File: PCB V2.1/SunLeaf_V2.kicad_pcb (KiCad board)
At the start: 2 copper layers, 118 parts, among them IC1 ESP_09, J1 20021121-00010C4LF, J10 S4B-PH-SM4-TB(LF)(SN), J11 S4B-PH-SM4-TB(LF)(SN), J12 S4B-PH-SM4-TB(LF)(SN), J13 S4B-PH-SM4-TB(LF)(SN), J14 S4B-PH-SM4-TB(LF)(SN), J15 S4B-PH-SM4-TB(LF)(SN), J16 S4B-PH-SM4-TB(LF)(SN), J2 0475890001-MicroUSBPort, J3 S2B-PH-SM4-TB(LF)(SN), J4 S3B-PH-SM4-TB(LF)(SN), J5 S4B-PH-SM4-TB(LF)(SN), J6 S4B-PH-SM4-TB(LF)(SN), J7 S4B-PH-SM4-TB(LF)(SN), J8 S4B-PH-SM4-TB(LF)(SN), J9 S4B-PH-SM4-TB(LF)(SN), P1 CONN_01X04, Q1 DMG2307L-7, Q2 DMG2307L-7, SW1 B3U-1000P, SW2 B3U-1000P, T1 1909763-1, U1 STM32F446RET6_-_TQFP64, U2 BQ24210DQCT, U3 AZ1117CR-3.3TRG1_1, U4 74HC4052D, U5 PCA9518DBQR, X1 ABM3B8.000MHZB2T, X2 ABS07-32.768KHZ-9-T

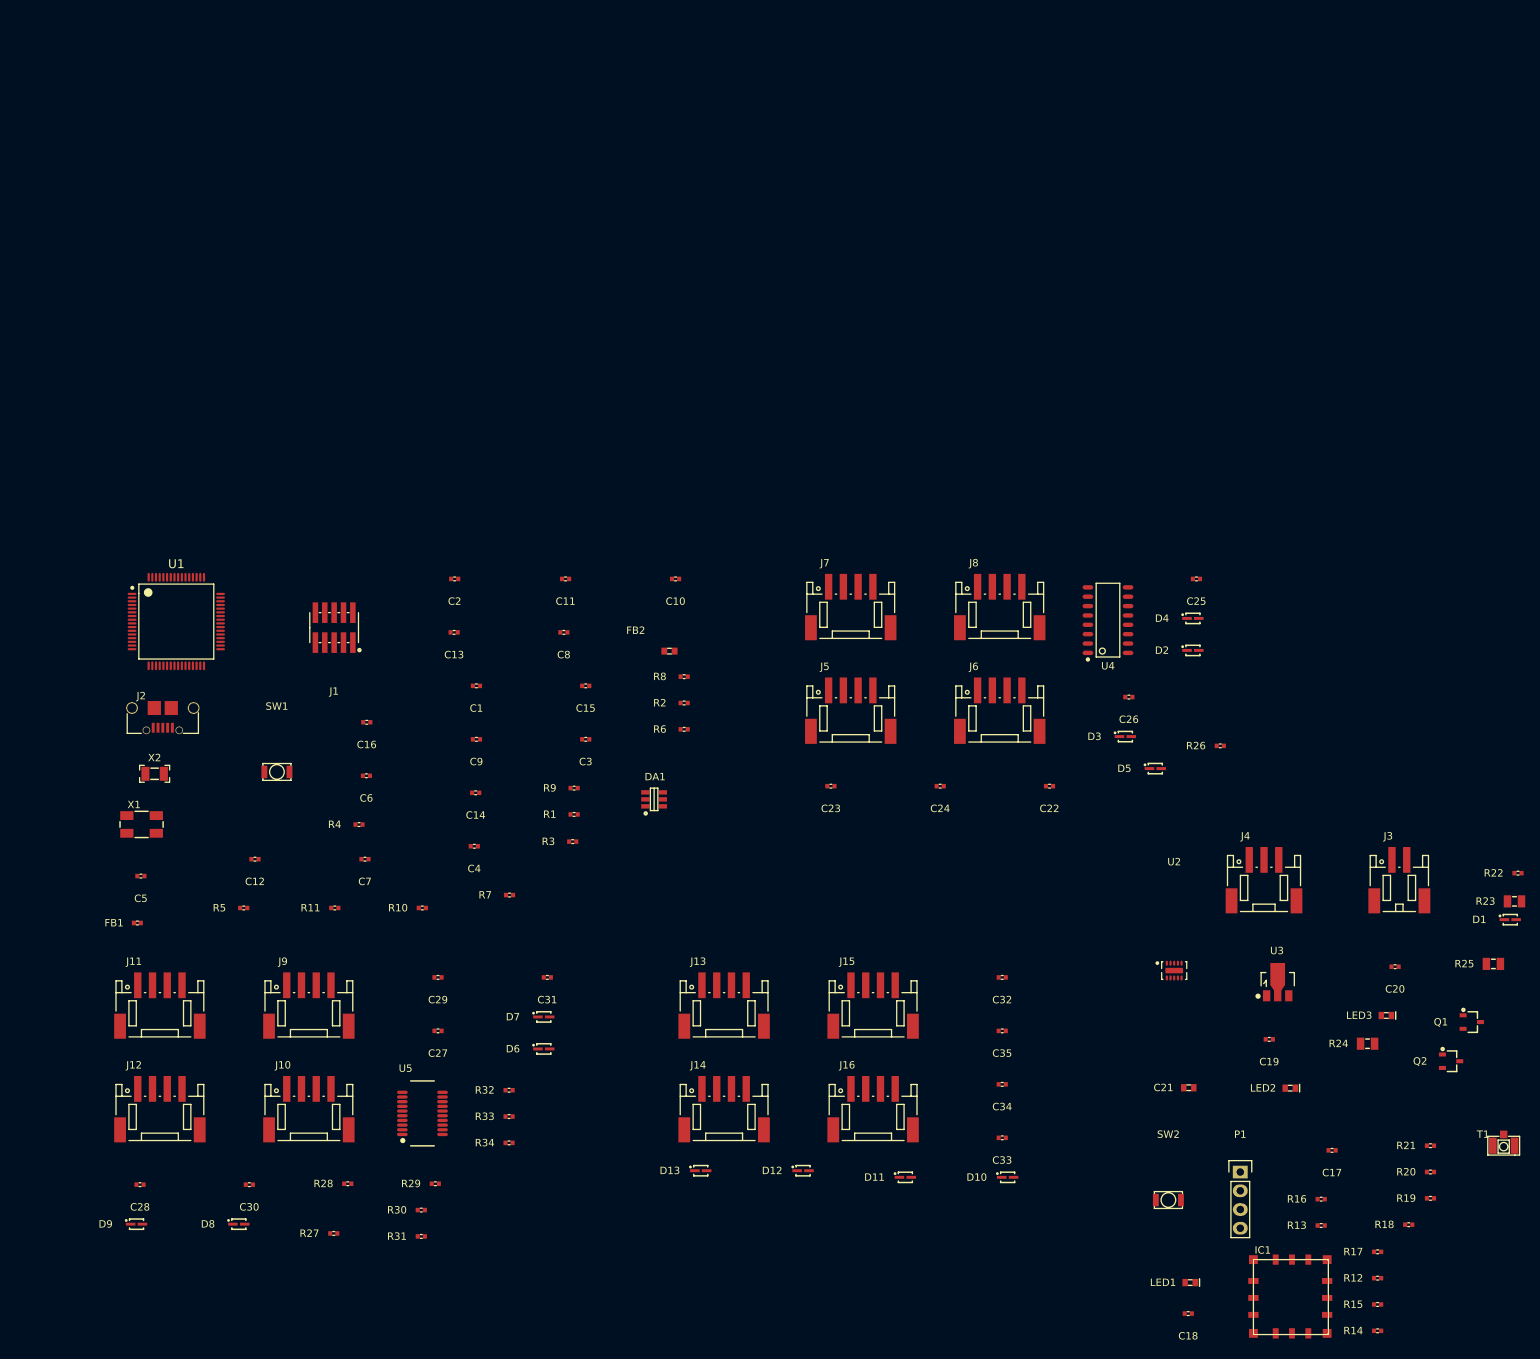
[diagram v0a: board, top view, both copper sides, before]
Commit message: Placement
Heavy progress on component placement in KiCAD for SunLEaf V2,
committing to save progress, nightly builds of KiCAD are very crash
prone.
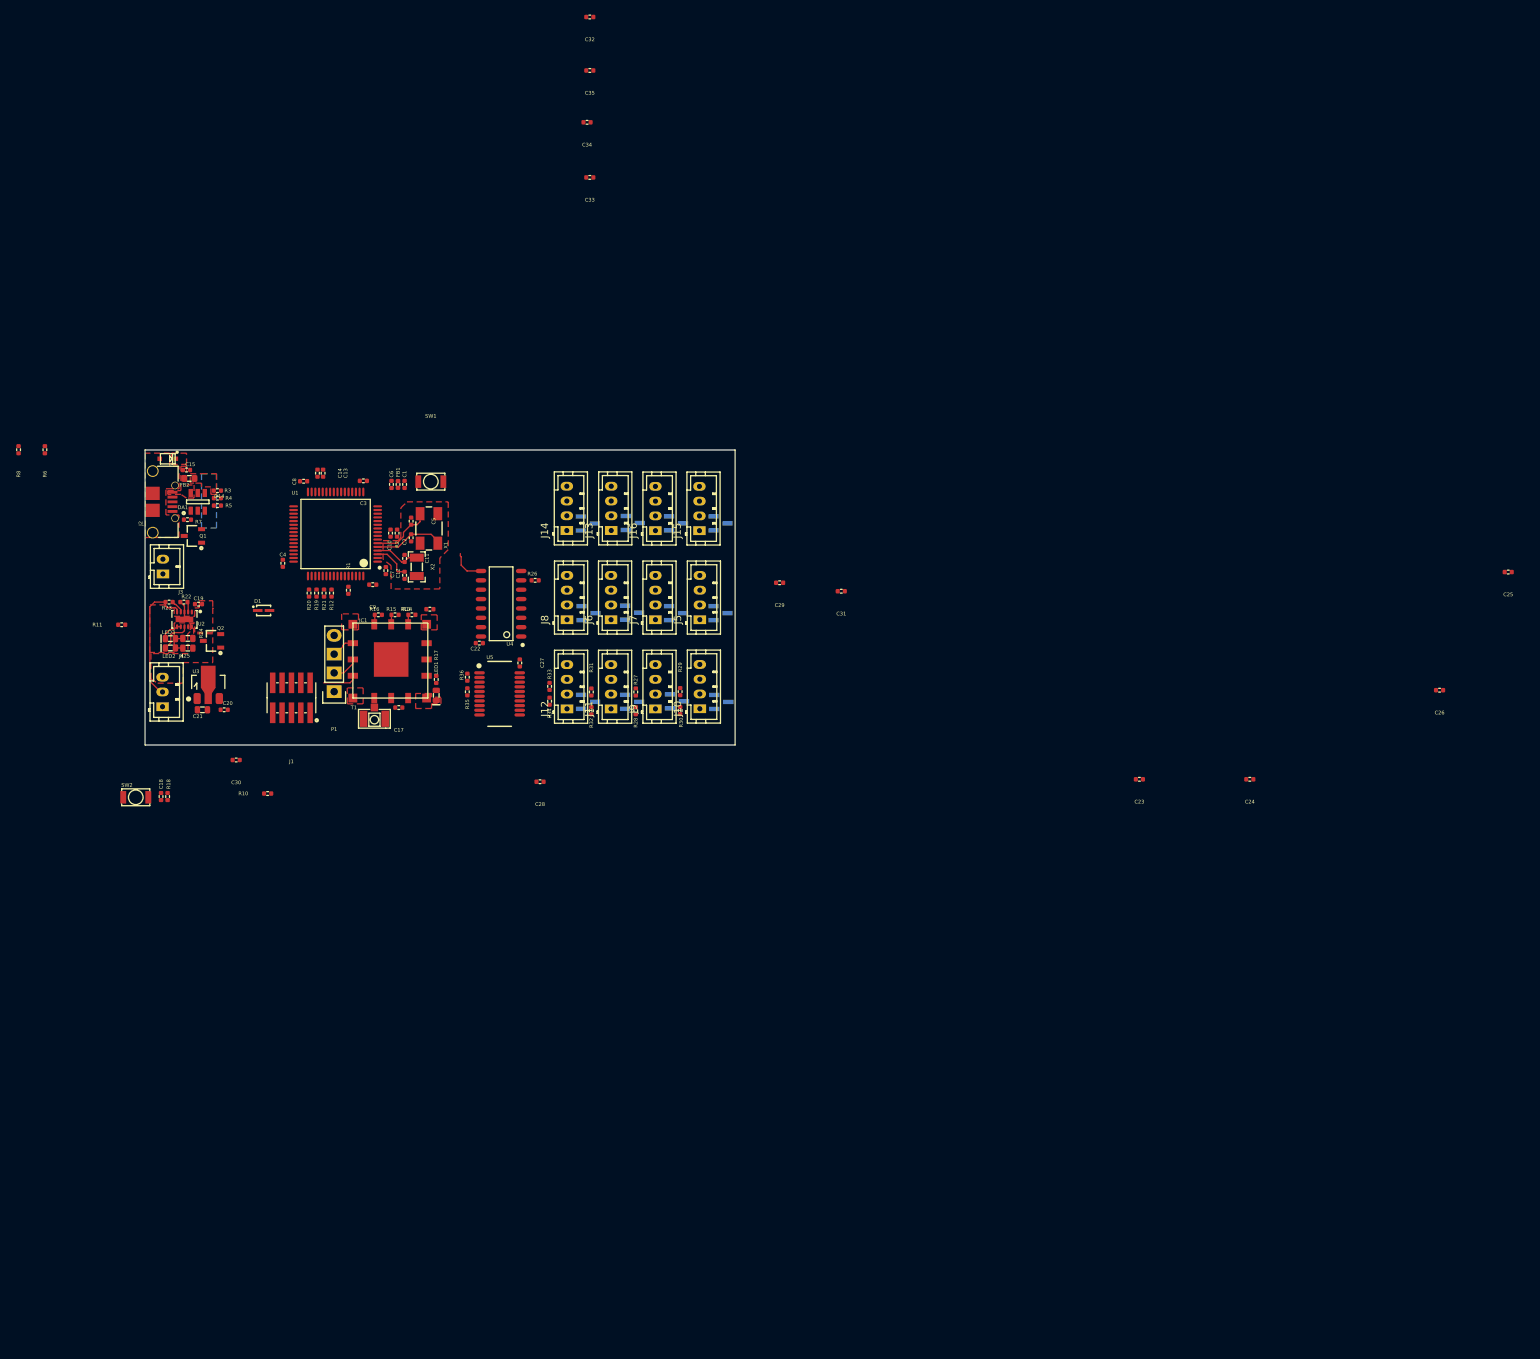
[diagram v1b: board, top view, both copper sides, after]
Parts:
- removed C16: CL05C470FB5NNNC, PCB_Footprints:C0402
- removed R9: RC1005F105CS, PCB_Footprints:R0402
- added D14: RSB39VTE-17, PCB_Footprints:RSB39VTE-17, F.Cu at (43.1, 31.2)
- added R35: RC1005F472CS, PCB_Footprints:R0402, F.Cu at (83.7, 62.8)
- added R36: RC1005F472CS, PCB_Footprints:R0402, F.Cu at (83.7, 60.8)
- D10, D11, D12, D13, D2, D3, D4, D5, D6, D7, D8, D9: footprint PCB_Footprints:BAT20JFILM -> PCB_Footprints:PESD3V3L2BT,215; moved to B.Cu
- J10, J11, J12, J13, J14, J15, J16, J5, J6, J7, J8, J9: value S4B-PH-SM4-TB(LF)(SN) -> B4B-PH-K-S(LF)(SN); footprint PCB_Footprints:S4B-PH-SM4-TB(LF)(SN) -> PCB_Footprints:B4B-PH-K-S(LF)(SN)
- J3: value S2B-PH-SM4-TB(LF)(SN) -> B2B-PH-K-S(LF)(SN); footprint PCB_Footprints:S2B-PH-SM4-TB(LF)(SN) -> PCB_Footprints:B2B-PH-K-S(LF)(SN)
- J4: value S3B-PH-SM4-TB(LF)(SN) -> B3B-PH-K-S(LF)(SN); footprint PCB_Footprints:S3B-PH-SM4-TB(LF)(SN) -> PCB_Footprints:B3B-PH-K-S(LF)(SN)
- R23: value RC2012F202CS -> RC1005F102CS; footprint PCB_Footprints:R0805 -> PCB_Footprints:R0402
- R24, R25: value RC2012F202CS -> RC1608J202CS; footprint PCB_Footprints:R0805 -> PCB_Footprints:R0603
- moved R23 186.9 mm to (43.3, 50.6), turned to 180 degrees
- moved Q1 185.5 mm to (46.5, 41.7), turned to 180 degrees
- moved R22 184.6 mm to (45.3, 50.6), turned to 180 degrees
- moved R25 182.4 mm to (45.8, 55.5)
- moved R18 178.0 mm to (43.1, 77.0), turned to 90 degrees
- moved Q2 177.4 mm to (49.1, 55.9), turned to 180 degrees
- moved D1 174.1 mm to (56.1, 51.8)
- moved J3 172.7 mm to (42.4, 46.8), turned to 90 degrees
- moved LED3 172.6 mm to (43.4, 55.6), turned to 180 degrees
- moved R19 171.9 mm to (63.2, 49.4), turned to 90 degrees
- moved R20 171.1 mm to (62.2, 49.4), turned to 90 degrees
- moved R12 169.5 mm to (65.3, 49.4), turned to 270 degrees
- moved R24 168.7 mm to (45.8, 56.9)
- moved R21 167.7 mm to (64.3, 49.4), turned to 90 degrees
- moved T1 163.7 mm to (71.1, 66.4)
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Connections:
- net Net-(D2-Pad1) renamed /UART Grove Sensors/UART_RX3
- net Net-(D2-Pad2) renamed /UART Grove Sensors/UART_TX3
- net Net-(D3-Pad1) renamed /UART Grove Sensors/UART_RX2
- net Net-(D3-Pad2) renamed /UART Grove Sensors/UART_TX2
- net Net-(D4-Pad1) renamed /UART Grove Sensors/UART_RX1
- net Net-(D4-Pad2) renamed /UART Grove Sensors/UART_TX1
- net Net-(D5-Pad1) renamed /UART Grove Sensors/UART_RX0
- net Net-(D5-Pad2) renamed /UART Grove Sensors/UART_TX0
- C17 pad 1: Net-(C17-Pad1) -> +3V3
- C19 pad 1: Net-(C19-Pad1) -> /MCU-STM32F446RET6/VBUS
- C8 pad 1: Net-(C8-Pad1) -> +3V3
- IC1 pad 15: Net-(C17-Pad1) -> +3V3
- J2 pad 5: Net-(J2-Pad5) -> GND
- J2 pad 6: Net-(C16-Pad1) -> Net-(D14-Pad1)
- J2 pad 8: Net-(C16-Pad1) -> Net-(D14-Pad1)
- J2 pad 9: Net-(C16-Pad1) -> Net-(D14-Pad1)
- J3 pad 1: Net-(J3-Pad1) -> GND
- J3 pad 2: GND -> Net-(J3-Pad2)
- J4 pad 1: /Power-System/BAT -> GND
- J4 pad 3: GND -> /Power-System/BAT
- P1 pad 1: Net-(IC1-Pad11) -> GND
- P1 pad 2: Net-(IC1-Pad10) -> Net-(IC1-Pad11)
- P1 pad 3: /WiFi-ESP8266-ESP-09/PGM_MODE -> Net-(IC1-Pad10)
- P1 pad 4: GND -> /WiFi-ESP8266-ESP-09/PGM_MODE
- Q1 pad 2: Net-(Q1-Pad2) -> /MCU-STM32F446RET6/VBUS
- Q1 pad 3: Net-(J3-Pad1) -> Net-(J3-Pad2)
- R23 pad 1: /Power-System/THERM -> Net-(R23-Pad1)
- R23 pad 2: Net-(R23-Pad2) -> /Power-System/THERM
- R24 pad 1: /Power-System/BAT -> Net-(LED2-Pad1)
- R24 pad 2: Net-(LED2-Pad1) -> /Power-System/BAT
- R25 pad 1: /Power-System/BAT -> Net-(LED3-Pad1)
- R25 pad 2: Net-(LED3-Pad1) -> /Power-System/BAT
- U1 pad 1: Net-(C8-Pad1) -> +3V3
- U2 pad 4: Net-(R23-Pad2) -> Net-(R23-Pad1)
- X1 pad 2: Net-(C5-Pad1) -> GND
- X1 pad 3: GND -> Net-(C5-Pad1)
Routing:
- net /Power-System/THERM: track 0.00 -> 17.5 mm
- net Net-(C2-Pad1): track 0.00 -> 9.54 mm
- net Net-(C5-Pad1): track 0.00 -> 8.37 mm
- net Net-(C11-Pad1): track 0.00 -> 6.22 mm
- net Net-(C12-Pad1): track 0.00 -> 5.18 mm
- net Net-(C18-Pad1): track 0.00 -> 4.69 mm
- net Net-(LED2-Pad2): track 0.00 -> 4.68 mm
- net /MCU-STM32F446RET6/USW_S1: track 0.00 -> 4.63 mm
- net Net-(IC1-Pad11): track 0.00 -> 3.63 mm
- net Net-(IC1-Pad10): track 0.00 -> 3.24 mm
- net Net-(LED3-Pad2): track 0.00 -> 3.10 mm
- net GND: track 0.00 -> 2.58 mm
- net Net-(R23-Pad1): track 0.00 -> 1.85 mm
- net Net-(R22-Pad1): track 0.00 -> 1.38 mm
- net /WiFi-ESP8266-ESP-09/PGM_MODE: track 0.00 -> 1.32 mm
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- added copper zone on B.Cu, net /MCU-STM32F446RET6/VBUS
- added copper zone on F.Cu, net /MCU-STM32F446RET6/VBUS
- added copper zone on F.Cu, net /Power-System/BAT
- added copper zone on F.Cu, net GND
- added copper zone on F.Cu, net Net-(C15-Pad2)
- added copper zone on F.Cu, net Net-(D14-Pad1)
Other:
- board outline added: 80 x 40 mm
- copper layers 2 -> 4
- net class All added: clearance 0.1524, trace_width 0.1778, via_dia 0.635, via_drill 0.3302
- net class Default: clearance 0.2 -> 0.1524; trace_width 0.25 -> 0.1778; via_dia 0.6 -> 0.635; via_drill 0.4 -> 0.3302
- rule pad_to_mask_clearance: 0.2 -> 0
- rule trace_clearance: 0.2 -> 0.1524
- rule trace_min: 0.2 -> 0.1778
- rule via_min_drill: 0.3 -> 0.3302
- rule via_min_size: 0.4 -> 0.635

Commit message: Placement progress
Placement is 99% done board is being resized. Next commit TVS diode
pairs will be fliped and the baord further resized.
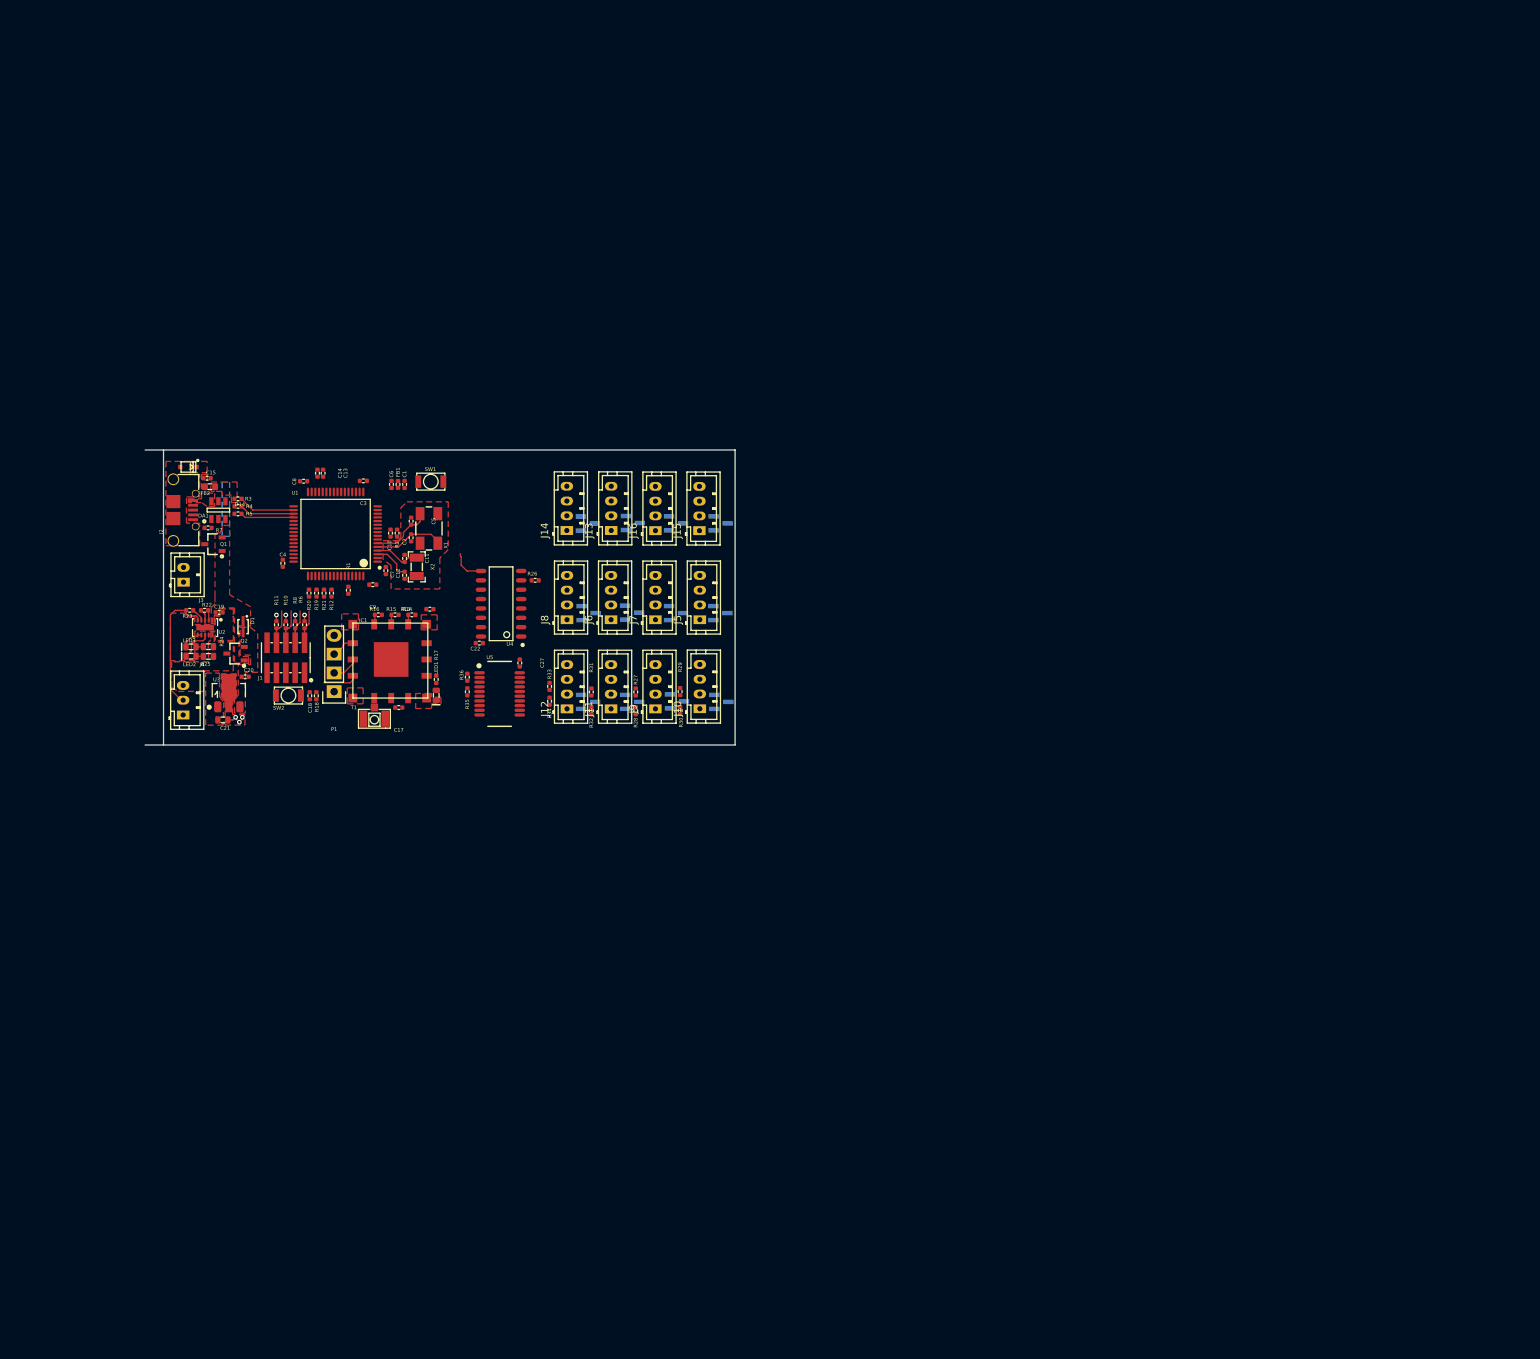
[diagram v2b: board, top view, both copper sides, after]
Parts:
- removed C23, C24, C25, C26, C28, C29, C30, C31, C32, C33, C34, C35: CL05B104JP5NNNC, PCB_Footprints:C0402
- moved R8 44.4 mm to (60.4, 53.7), turned to 270 degrees
- moved R6 42.5 mm to (61.6, 53.7), turned to 270 degrees
- moved SW2 24.9 mm to (59.4, 63.3)
- moved C18 24.4 mm to (62.3, 63.3)
- moved R18 24.4 mm to (63.2, 63.3)
- moved R10 23.0 mm to (59.1, 53.7), turned to 270 degrees
- moved R11 21.0 mm to (57.8, 53.7), turned to 270 degrees
- moved J1 5.49 mm to (59.1, 58.2)
- moved C20 5.30 mm to (53.6, 60.8)
- moved Q2 3.63 mm to (52.3, 57.6)
- moved D1 3.54 mm to (53.3, 53.9), turned to 270 degrees
- moved C21 3.09 mm to (50.5, 66.6)
- moved J4 3.01 mm to (45.2, 65.9)
- moved J3 3.01 mm to (45.2, 47.9)
- moved LED2 3.01 mm to (46.2, 58.0)
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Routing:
- net Net-(R3-Pad1): track 0.00 -> 7.68 mm
- net Net-(R4-Pad1): track 0.00 -> 7.46 mm
- net Net-(R5-Pad1): track 0.00 -> 7.25 mm
- net +3V3: track 0.00 -> 6.25 mm, vias 0 -> 7
- net /MCU-STM32F446RET6/SWO_TDO: track 0.00 -> 4.87 mm
- net /MCU-STM32F446RET6/SWO_TDI: track 0.00 -> 4.85 mm
- net /MCU-STM32F446RET6/SWCLK_TCK: track 0.00 -> 4.59 mm
- net /MCU-STM32F446RET6/SWDIO_TMS: track 0.00 -> 4.57 mm
- added copper zone on F.Cu, net +3V3
- added copper zone on F.Cu, net Net-(C20-Pad1)
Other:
- outline, holes or cut-outs redrawn
